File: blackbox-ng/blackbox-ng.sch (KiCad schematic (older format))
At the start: 0 parts

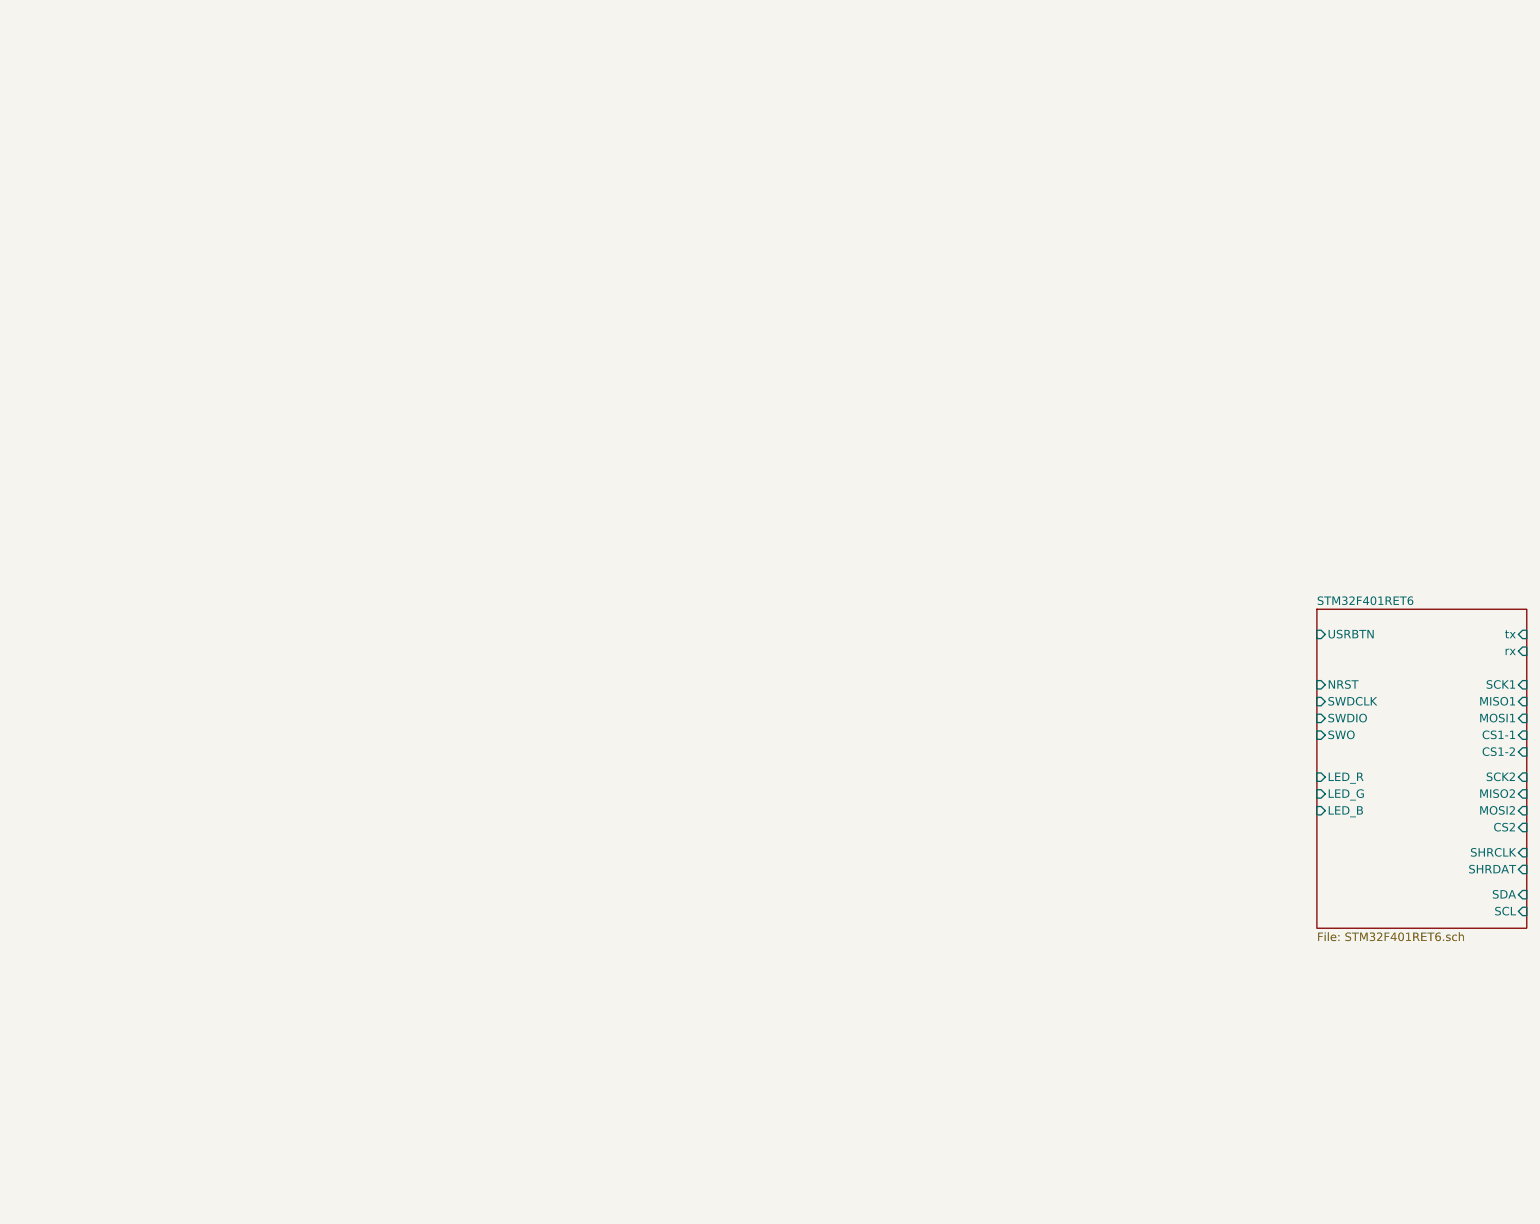
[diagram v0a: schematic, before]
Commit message: add linear regulator
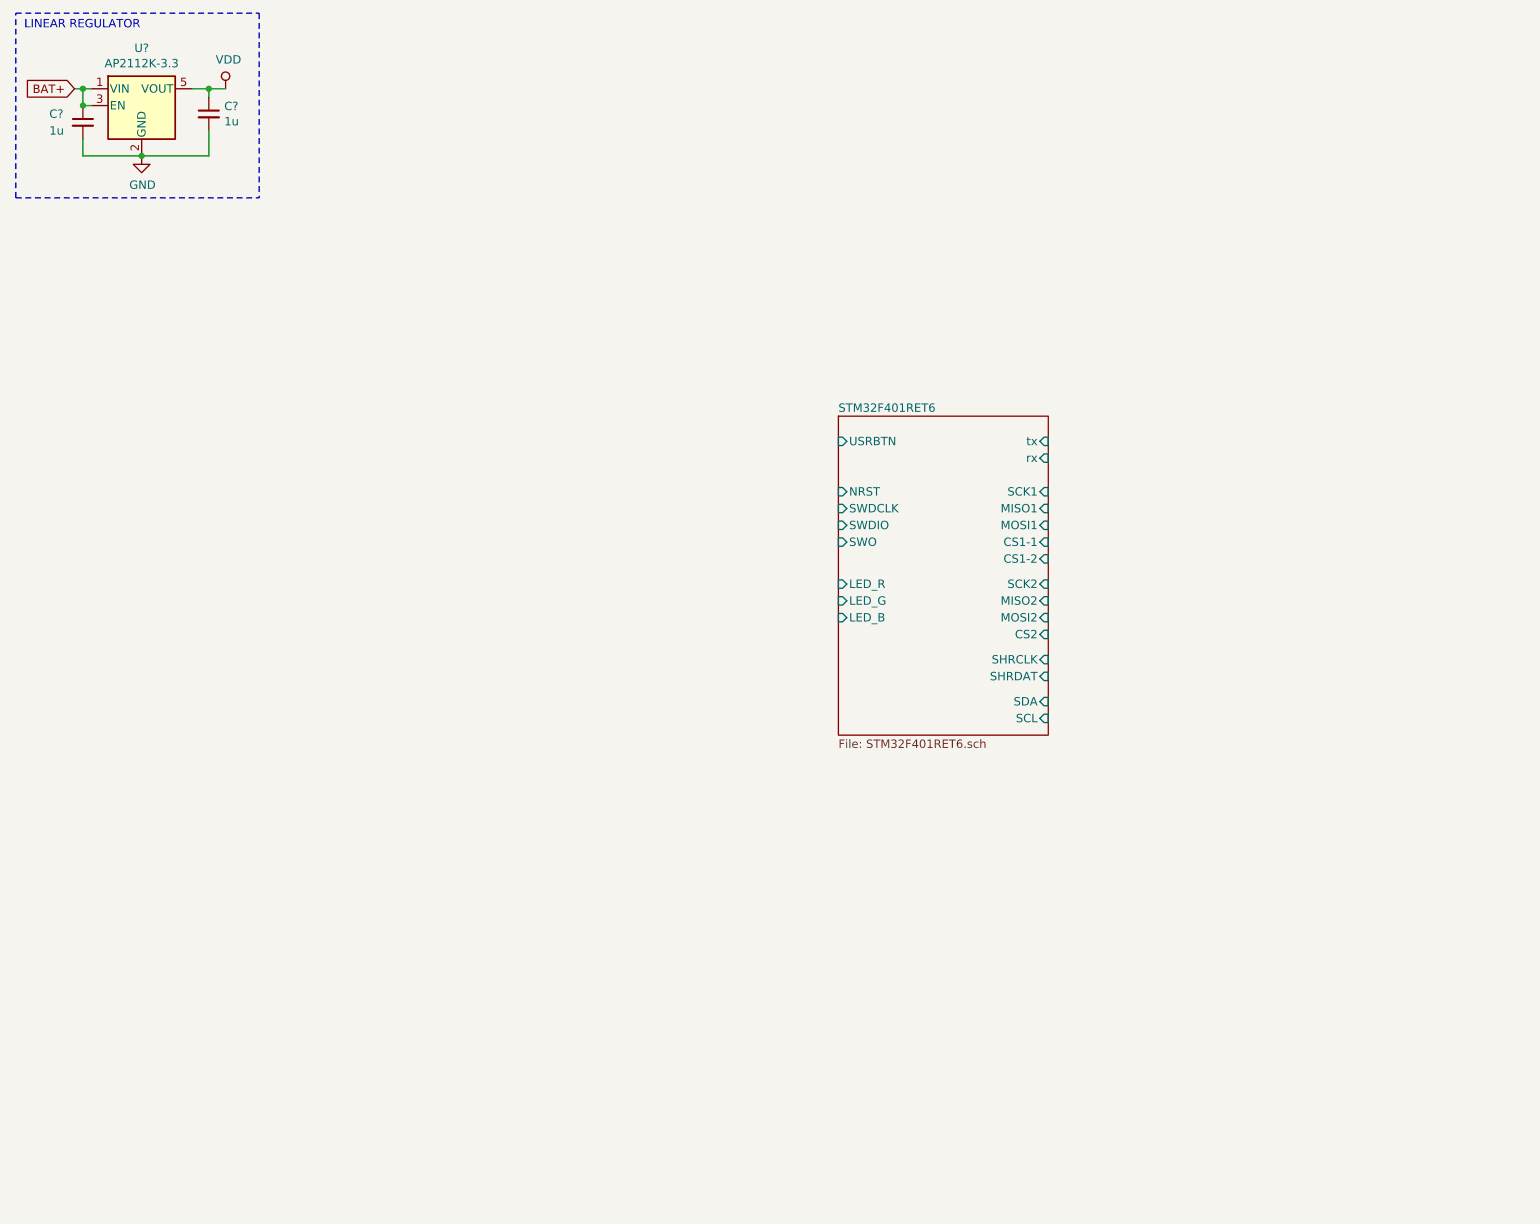
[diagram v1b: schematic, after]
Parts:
- added C? (x2): 1u, symbol Device:C_Small
- added U?: AP2112K-3.3, Package_TO_SOT_SMD:SOT-23-5, symbol Regulator_Linear:AP2112K-3.3
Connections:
- new net BAT+: C?.1, U?.1 (VIN), U?.3 (EN)
- new net GND: C?.2, C?.2, U?.2 (GND)
- new net VDD: C?.1, U?.5 (VOUT)
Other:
- note added: "LINEAR REGULATOR"
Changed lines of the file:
@@
 $EndDescr
 $Sheet
-S 8350 4150 1250 1900
+S 5500 3000 1250 1900
 U 5DDEE5E2
 F0 "STM32F401RET6" 50
 F1 "STM32F401RET6.sch" 50
-F2 "NRST" I L 8350 4600 50
-F3 "USRBTN" I L 8350 4300 50
-F4 "tx" I R 9600 4300 50
-F5 "rx" I R 9600 4400 50
-F6 "SCK1" I R 9600 4600 50
-F7 "MISO1" I R 9600 4700 50
-F8 "MOSI1" I R 9600 4800 50
-F9 "CS1-1" I R 9600 4900 50
-F10 "CS1-2" I R 9600 5000 50
-F11 "MOSI2" I R 9600 5350 50
-F12 "MISO2" I R 9600 5250 50
-F13 "SCK2" I R 9600 5150 50
-F14 "CS2" I R 9600 5450 50
-F15 "SHRCLK" I R 9600 5600 50
-F16 "SHRDAT" I R 9600 5700 50
-F17 "LED_R" I L 8350 5150 50
-F18 "LED_B" I L 8350 5350 50
-F19 "LED_G" I L 8350 5250 50
-F20 "SWDIO" I L 8350 4800 50
-F21 "SWDCLK" I L 8350 4700 50
-F22 "SWO" I L 8350 4900 50
-F23 "SCL" I R 9600 5950 50
-F24 "SDA" I R 9600 5850 50
+F2 "NRST" I L 5500 3450 50
+F3 "USRBTN" I L 5500 3150 50
+F4 "tx" I R 6750 3150 50
+F5 "rx" I R 6750 3250 50
+F6 "SCK1" I R 6750 3450 50
+F7 "MISO1" I R 6750 3550 50
+F8 "MOSI1" I R 6750 3650 50
+F9 "CS1-1" I R 6750 3750 50
+F10 "CS1-2" I R 6750 3850 50
+F11 "MOSI2" I R 6750 4200 50
+F12 "MISO2" I R 6750 4100 50
+F13 "SCK2" I R 6750 4000 50
+F14 "CS2" I R 6750 4300 50
+F15 "SHRCLK" I R 6750 4450 50
+F16 "SHRDAT" I R 6750 4550 50
+F17 "LED_R" I L 5500 4000 50
+F18 "LED_B" I L 5500 4200 50
+F19 "LED_G" I L 5500 4100 50
+F20 "SWDIO" I L 5500 3650 50
+F21 "SWDCLK" I L 5500 3550 50
+F22 "SWO" I L 5500 3750 50
+F23 "SCL" I R 6750 4800 50
+F24 "SDA" I R 6750 4700 50
 $EndSheet
+$Comp
+L Regulator_Linear:AP2112K-3.3 U?
+U 1 1 5DEFD5A3
+P 1350 1150
+F 0 "U?" H 1350 1492 50  0000 C CNN
+F 1 "AP2112K-3.3" H 1350 1401 50  0000 C CNN
+F 2 "Package_TO_SOT_SMD:SOT-23-5" H 1350 1475 50  0001 C CNN
+F 3 "https://www.diodes.com/assets/Datasheets/AP2112.pdf" H 1350 1250 50  0001 C CNN
+	1    1350 1150
+	1    0    0    -1
+$EndComp
+Text GLabel 950  1050 0    50   Input ~ 0
+BAT+
+Wire Wire Line
+	950  1050 1000 1050
+Wire Wire Line
+	1000 1050 1000 1150
+Wire Wire Line
+	1000 1150 1050 1150
+Connection ~ 1000 1050
+Wire Wire Line
+	1000 1050 1050 1050
+$Comp
+L power:GND #PWR?
+U 1 1 5DF00632
+P 1350 1450
+F 0 "#PWR?" H 1350 1200 50  0001 C CNN
+F 1 "GND" H 1355 1277 50  0000 C CNN
+F 2 "" H 1350 1450 50  0001 C CNN
+F 3 "" H 1350 1450 50  0001 C CNN
+	1    1350 1450
+	1    0    0    -1
+$EndComp
+$Comp
+L power:VDD #PWR?
+U 1 1 5DF00BA7
+P 1850 1050
+F 0 "#PWR?" H 1850 900 50  0001 C CNN
+F 1 "VDD" H 1867 1223 50  0000 C CNN
+F 2 "" H 1850 1050 50  0001 C CNN
+F 3 "" H 1850 1050 50  0001 C CNN
+	1    1850 1050
+	1    0    0    -1
+$EndComp
+Wire Wire Line
+	1650 1050 1750 1050
+$Comp
+L Device:C_Small C?
+U 1 1 5DF01E03
+P 1750 1200
+F 0 "C?" H 1842 1246 50  0000 L CNN
+F 1 "1u" H 1842 1155 50  0000 L CNN
+F 2 "" H 1750 1200 50  0001 C CNN
+F 3 "~" H 1750 1200 50  0001 C CNN
+	1    1750 1200
+	1    0    0    -1
+$EndComp
+Wire Wire Line
+	1750 1050 1750 1100
+Connection ~ 1750 1050
+Wire Wire Line
+	1750 1050 1850 1050
+Wire Wire Line
+	1750 1300 1750 1450
+Wire Wire Line
+	1750 1450 1350 1450
+Connection ~ 1350 1450
+$Comp
+L Device:C_Small C?
+U 1 1 5DF02B2B
+P 1000 1250
+F 0 "C?" H 800 1300 50  0000 L CNN
+F 1 "1u" H 800 1200 50  0000 L CNN
+F 2 "" H 1000 1250 50  0001 C CNN
+F 3 "~" H 1000 1250 50  0001 C CNN
+	1    1000 1250
+	1    0    0    -1
+$EndComp
+Connection ~ 1000 1150
+Wire Wire Line
+	1000 1350 1000 1450
+Wire Wire Line
+	1000 1450 1350 1450
+Wire Notes Line
+	600  600  2050 600
+Wire Notes Line
+	2050 600  2050 1700
+Wire Notes Line
+	600  1700 600  600
+Wire Notes Line
+	600  1700 2050 1700
+Text Notes 650  700  0    50   ~ 0
+LINEAR REGULATOR
 $EndSCHEMATC

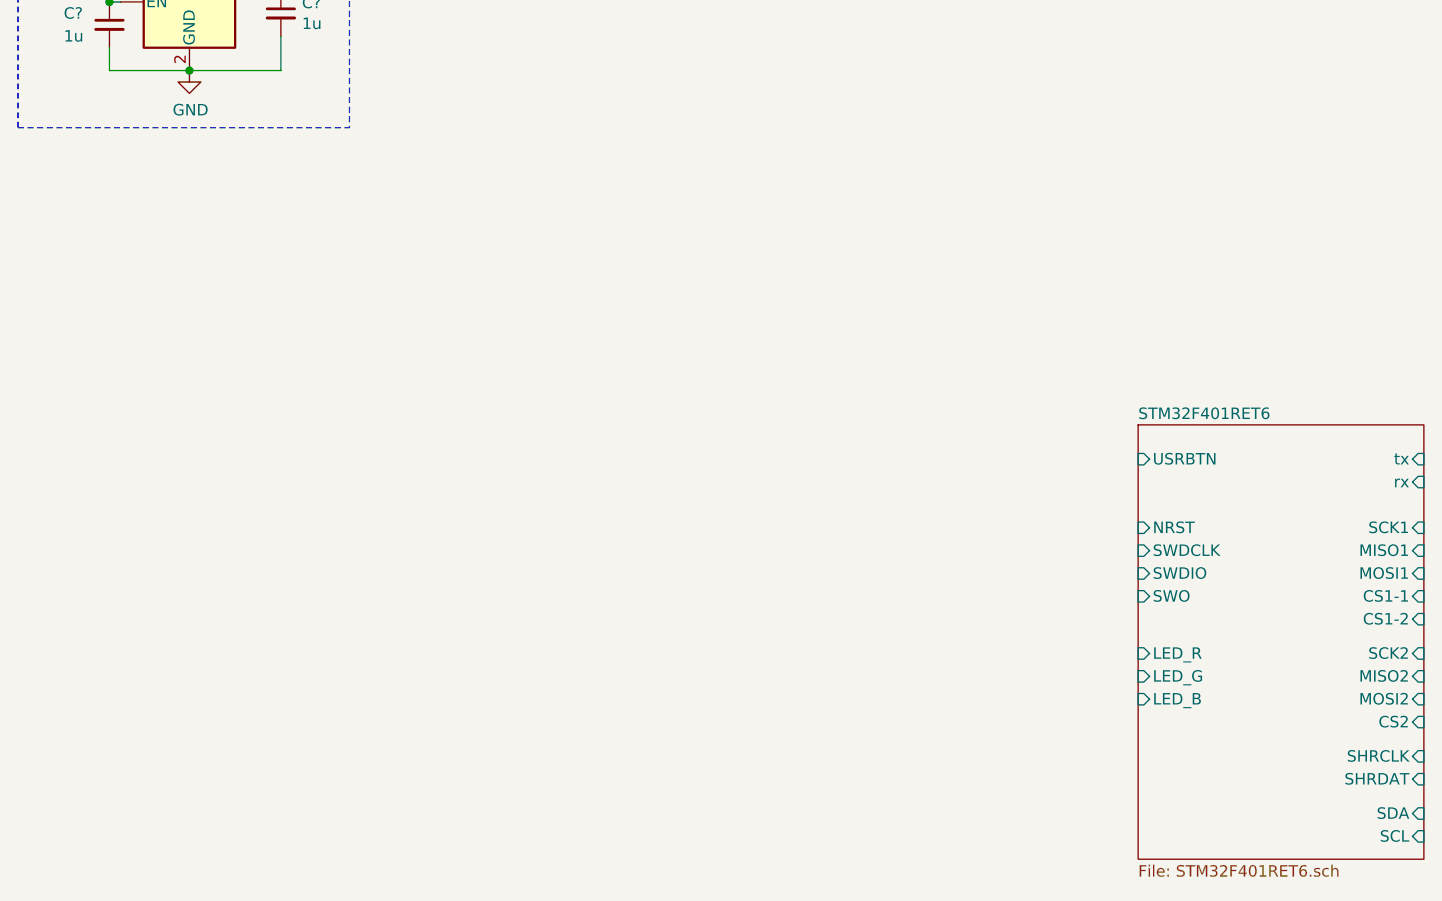
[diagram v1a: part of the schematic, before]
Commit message: add battery
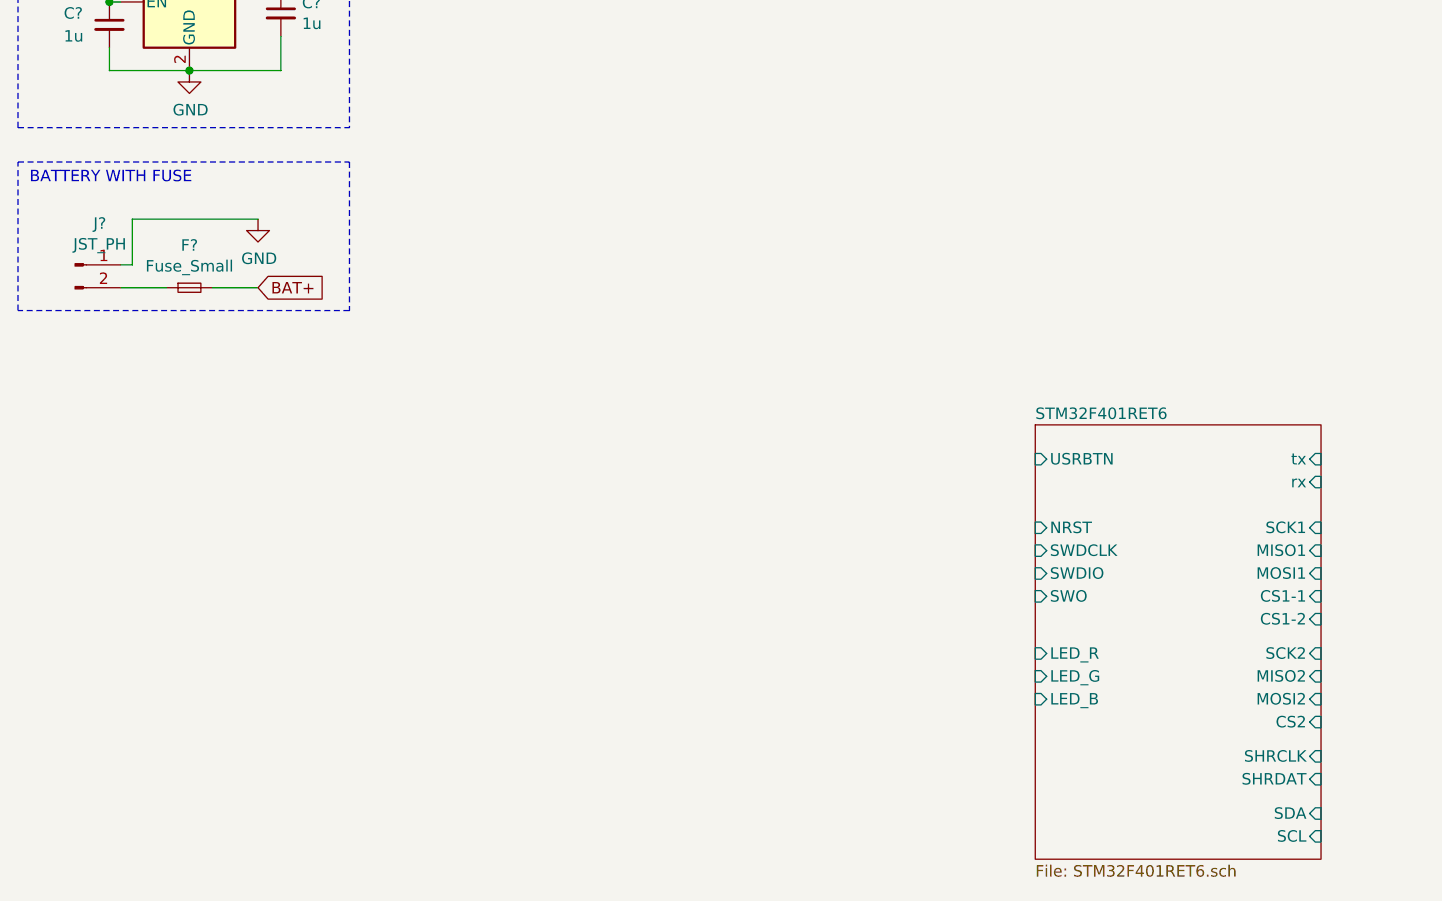
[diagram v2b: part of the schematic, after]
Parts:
- added F?: Fuse_Small, symbol Device:Fuse_Small
- added J?: JST_PH, symbol Connector:Conn_01x02_Male
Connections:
- net BAT+: now also F?.2
- net GND: now also J?.1 (Pin_1)
- new net: F?.1, J?.2 (Pin_2)
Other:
- note added: "BATTERY WITH FUSE"
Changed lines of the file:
@@
 $EndDescr
 $Sheet
-S 5500 3000 1250 1900
+S 5050 3000 1250 1900
 U 5DDEE5E2
 F0 "STM32F401RET6" 50
 F1 "STM32F401RET6.sch" 50
-F2 "NRST" I L 5500 3450 50
-F3 "USRBTN" I L 5500 3150 50
-F4 "tx" I R 6750 3150 50
-F5 "rx" I R 6750 3250 50
-F6 "SCK1" I R 6750 3450 50
-F7 "MISO1" I R 6750 3550 50
-F8 "MOSI1" I R 6750 3650 50
-F9 "CS1-1" I R 6750 3750 50
-F10 "CS1-2" I R 6750 3850 50
-F11 "MOSI2" I R 6750 4200 50
-F12 "MISO2" I R 6750 4100 50
-F13 "SCK2" I R 6750 4000 50
-F14 "CS2" I R 6750 4300 50
-F15 "SHRCLK" I R 6750 4450 50
-F16 "SHRDAT" I R 6750 4550 50
-F17 "LED_R" I L 5500 4000 50
-F18 "LED_B" I L 5500 4200 50
-F19 "LED_G" I L 5500 4100 50
-F20 "SWDIO" I L 5500 3650 50
-F21 "SWDCLK" I L 5500 3550 50
-F22 "SWO" I L 5500 3750 50
-F23 "SCL" I R 6750 4800 50
-F24 "SDA" I R 6750 4700 50
+F2 "NRST" I L 5050 3450 50
+F3 "USRBTN" I L 5050 3150 50
+F4 "tx" I R 6300 3150 50
+F5 "rx" I R 6300 3250 50
+F6 "SCK1" I R 6300 3450 50
+F7 "MISO1" I R 6300 3550 50
+F8 "MOSI1" I R 6300 3650 50
+F9 "CS1-1" I R 6300 3750 50
+F10 "CS1-2" I R 6300 3850 50
+F11 "MOSI2" I R 6300 4200 50
+F12 "MISO2" I R 6300 4100 50
+F13 "SCK2" I R 6300 4000 50
+F14 "CS2" I R 6300 4300 50
+F15 "SHRCLK" I R 6300 4450 50
+F16 "SHRDAT" I R 6300 4550 50
+F17 "LED_R" I L 5050 4000 50
+F18 "LED_B" I L 5050 4200 50
+F19 "LED_G" I L 5050 4100 50
+F20 "SWDIO" I L 5050 3650 50
+F21 "SWDCLK" I L 5050 3550 50
+F22 "SWO" I L 5050 3750 50
+F23 "SCL" I R 6300 4800 50
+F24 "SDA" I R 6300 4700 50
 $EndSheet
 $Comp
@@
 Text Notes 650  700  0    50   ~ 0
 LINEAR REGULATOR
+$Comp
+L Connector:Conn_01x02_Male J?
+U 1 1 5DF0FA0D
+P 850 2300
+F 0 "J?" H 958 2481 50  0000 C CNN
+F 1 "JST_PH" H 958 2390 50  0000 C CNN
+F 2 "" H 850 2300 50  0001 C CNN
+F 3 "~" H 850 2300 50  0001 C CNN
+	1    850  2300
+	1    0    0    -1
+$EndComp
+$Comp
+L Device:Fuse_Small F?
+U 1 1 5DF106B0
+P 1350 2400
+F 0 "F?" H 1350 2585 50  0000 C CNN
+F 1 "Fuse_Small" H 1350 2494 50  0000 C CNN
+F 2 "" H 1350 2400 50  0001 C CNN
+F 3 "~" H 1350 2400 50  0001 C CNN
+	1    1350 2400
+	1    0    0    -1
+$EndComp
+Wire Wire Line
+	1050 2400 1250 2400
+Text GLabel 1650 2400 2    50   Input ~ 0
+BAT+
+$Comp
+L power:GND #PWR?
+U 1 1 5DF1110C
+P 1650 2100
+F 0 "#PWR?" H 1650 1850 50  0001 C CNN
+F 1 "GND" H 1655 1927 50  0000 C CNN
+F 2 "" H 1650 2100 50  0001 C CNN
+F 3 "" H 1650 2100 50  0001 C CNN
+	1    1650 2100
+	1    0    0    -1
+$EndComp
+Wire Wire Line
+	1050 2300 1100 2300
+Wire Wire Line
+	1100 2300 1100 2100
+Wire Wire Line
+	1100 2100 1650 2100
+Wire Wire Line
+	1450 2400 1650 2400
+Wire Notes Line
+	600  1850 2050 1850
+Wire Notes Line
+	2050 1850 2050 2500
+Wire Notes Line
+	2050 2500 600  2500
+Wire Notes Line
+	600  2500 600  1850
+Text Notes 650  1950 0    50   ~ 0
+BATTERY WITH FUSE
 $EndSCHEMATC
